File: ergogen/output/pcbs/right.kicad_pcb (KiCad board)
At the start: 2 copper layers, 140.9 x 96.1 mm, 85 parts

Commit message: add: component placement, niceview, mirror pcb
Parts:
- moved LED1 280.0 mm to (330.0, 177.3)
- moved LED2 280.0 mm to (330.0, 159.3)
- moved LED3 280.0 mm to (330.0, 141.3)
- moved S1 280.0 mm to (330.0, 182.0)
- moved S2 280.0 mm to (330.0, 164.0)
- moved S3 280.0 mm to (330.0, 146.0)
- moved D1 264.0 mm to (322.0, 177.6), turned to -90 degrees
- moved D2 264.0 mm to (322.0, 159.6), turned to -90 degrees
- moved D3 264.0 mm to (322.0, 141.6), turned to -90 degrees
- moved H2 262.0 mm to (321.0, 144.0)
- moved LED26 262.0 mm to (321.0, 151.5)
- moved LED27 262.0 mm to (321.0, 172.5)
- moved H3 261.6 mm to (320.8, 188.0)
- moved LED4 244.0 mm to (312.0, 173.3)
- moved LED5 244.0 mm to (312.0, 155.3)
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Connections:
- net close_thumb renamed mirror_close_thumb
- net home_thumb renamed mirror_home_thumb
- net index_bottom renamed mirror_index_bottom
- net index_home renamed mirror_index_home
- net index_top renamed mirror_index_top
- net inner_bottom renamed mirror_inner_bottom
- net inner_home renamed mirror_inner_home
- net inner_thumb renamed mirror_inner_thumb
- net inner_top renamed mirror_inner_top
- net middle_bottom renamed mirror_middle_bottom
- net middle_home renamed mirror_middle_home
- net middle_top renamed mirror_middle_top
- net outer_bottom renamed mirror_outer_bottom
- net outer_home renamed mirror_outer_home
- net outer_thumb renamed mirror_outer_thumb
- net outer_top renamed mirror_outer_top
- net pinky_bottom renamed mirror_pinky_bottom
- net pinky_home renamed mirror_pinky_home
- net pinky_top renamed mirror_pinky_top
- net ring_bonus renamed mirror_ring_bonus
- net ring_bottom renamed mirror_ring_bottom
- net ring_home renamed mirror_ring_home
- net ring_top renamed mirror_ring_top
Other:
- outline, holes or cut-outs redrawn

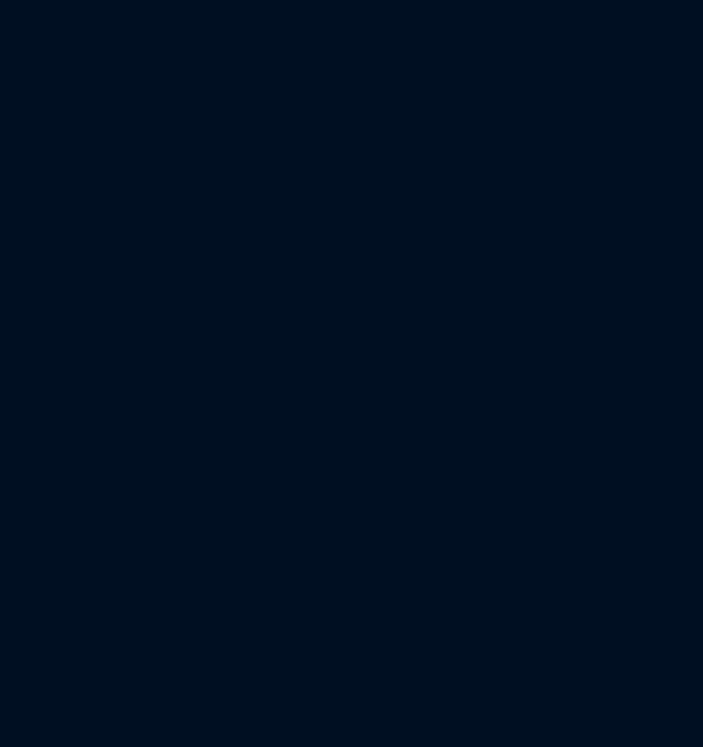
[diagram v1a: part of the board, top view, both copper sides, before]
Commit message: fix: ergogen lio logo
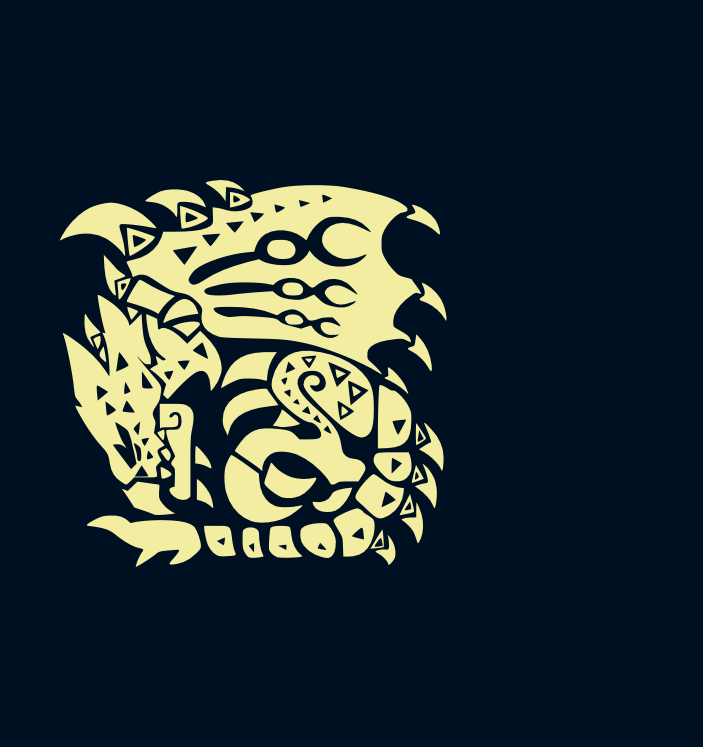
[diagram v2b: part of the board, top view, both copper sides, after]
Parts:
- added G: Lio, custom:lio, F.Cu at (156.2, 173.4)

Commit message: add: routing paras, position adjustments
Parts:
- G: moved to B.Cu
- moved D23 71.4 mm to (325.0, 141.6)
- moved D18 69.7 mm to (276.0, 182.6)
- moved D22 59.3 mm to (253.6, 142.6), turned to -90 degrees
- moved D13 44.8 mm to (250.0, 160.6)
- moved D15 43.9 mm to (232.0, 164.6)
- moved D6 43.9 mm to (286.0, 177.6)
- moved D10 36.7 mm to (268.0, 155.6)
- moved D3 36.7 mm to (304.0, 173.6)
- moved D14 36.0 mm to (250.0, 124.6)
- moved D20 20.9 mm to (237.1, 183.2), turned to -75 degrees
- moved D21 20.9 mm to (217.0, 189.3), turned to -60 degrees
- moved D11 18.0 mm to (268.0, 137.6)
- moved D12 18.0 mm to (268.0, 119.6)
- moved D16 18.0 mm to (232.0, 146.6)
- moved D17 18.0 mm to (232.0, 128.6)
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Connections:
- D1 pad 1: (no net) -> P022
- D10 pad 1: (no net) -> P022
- D10 pad 2: mirror_ring_top -> mirror_middle_bottom
- D11 pad 1: (no net) -> P020
- D11 pad 2: mirror_middle_bottom -> mirror_middle_home
- D12 pad 1: (no net) -> P017
- D12 pad 2: mirror_middle_home -> mirror_middle_top
- D13 pad 1: (no net) -> P022
- D13 pad 2: mirror_middle_top -> mirror_index_bottom
- D14 pad 1: (no net) -> P017
- D14 pad 2: mirror_index_bottom -> mirror_index_top
- D15 pad 1: (no net) -> P022
- D15 pad 2: mirror_index_top -> mirror_inner_bottom
- D16 pad 1: (no net) -> P020
- D16 pad 2: mirror_inner_bottom -> mirror_inner_home
- D17 pad 1: (no net) -> P017
- D17 pad 2: mirror_inner_home -> mirror_inner_top
- D18 pad 1: (no net) -> P017
- D18 pad 2: mirror_inner_top -> mirror_inner_thumb
- D19 pad 1: (no net) -> P017
- D19 pad 2: mirror_inner_thumb -> mirror_close_thumb
- D2 pad 1: (no net) -> P020
- D20 pad 1: (no net) -> P017
- D20 pad 2: mirror_close_thumb -> mirror_home_thumb
- D21 pad 1: (no net) -> P017
- D21 pad 2: mirror_home_thumb -> mirror_outer_thumb
- D22 pad 1: (no net) -> P020
- D22 pad 2: mirror_outer_thumb -> mirror_index_home
- D23 pad 1: (no net) -> P017
- D23 pad 2: mirror_index_home -> mirror_outer_top
- D3 pad 1: (no net) -> P022
- D3 pad 2: mirror_outer_top -> mirror_pinky_bottom
- D4 pad 1: (no net) -> P020
- D4 pad 2: mirror_pinky_bottom -> mirror_pinky_home
- D5 pad 1: (no net) -> P017
- D5 pad 2: mirror_pinky_home -> mirror_pinky_top
- D6 pad 1: (no net) -> P024
- D6 pad 2: mirror_pinky_top -> mirror_ring_bonus
- D7 pad 1: (no net) -> P022
- D7 pad 2: mirror_ring_bonus -> mirror_ring_bottom
- D8 pad 1: (no net) -> P020
- D8 pad 2: mirror_ring_bottom -> mirror_ring_home
- D9 pad 1: (no net) -> P017
- D9 pad 2: mirror_ring_home -> mirror_ring_top
- LED1 pad 2: (no net) -> LED_23
- LED1 pad 4: (no net) -> LED_22
- LED10 pad 2: (no net) -> LED_14
- LED10 pad 4: (no net) -> LED_13
- LED11 pad 2: (no net) -> LED_11
- LED11 pad 4: (no net) -> LED_10
- LED12 pad 2: (no net) -> LED_12
- LED12 pad 4: (no net) -> LED_11
- LED13 pad 2: (no net) -> LED_13
- LED13 pad 4: (no net) -> LED_12
- LED14 pad 2: (no net) -> LED_7
- LED14 pad 4: (no net) -> LED_6
- LED15 pad 2: (no net) -> LED_6
- LED15 pad 4: (no net) -> LED_5
- LED16 pad 2: (no net) -> LED_5
- LED16 pad 4: (no net) -> LED_4
- LED17 pad 2: (no net) -> LED_2
- LED17 pad 4: (no net) -> LED_1
- LED18 pad 2: (no net) -> LED_3
- LED18 pad 4: (no net) -> LED_2
- LED19 pad 2: (no net) -> LED_4
- LED19 pad 4: (no net) -> LED_3
- LED2 pad 2: (no net) -> LED_22
- LED2 pad 4: (no net) -> LED_21
- LED20 pad 2: (no net) -> LED_10
- LED20 pad 4: (no net) -> LED_9
- LED21 pad 2: (no net) -> LED_9
- LED21 pad 4: (no net) -> LED_8
- LED22 pad 2: (no net) -> LED_8
- LED22 pad 4: (no net) -> LED_7
- LED23 pad 2: (no net) -> LED_1
- LED23 pad 4: (no net) -> ULED_6
- LED24 pad 4: LED -> P006
- LED3 pad 2: (no net) -> LED_21
- LED3 pad 4: (no net) -> LED_20
- LED4 pad 2: (no net) -> LED_18
- LED4 pad 4: (no net) -> LED_17
- LED5 pad 2: (no net) -> LED_19
- LED5 pad 4: (no net) -> LED_18
- LED6 pad 2: (no net) -> LED_20
- LED6 pad 4: (no net) -> LED_19
- LED7 pad 2: (no net) -> LED_17
- LED7 pad 4: (no net) -> LED_16
- LED8 pad 2: (no net) -> LED_16
- LED8 pad 4: (no net) -> LED_15
- LED9 pad 2: (no net) -> LED_15
- LED9 pad 4: (no net) -> LED_14
- S1 pad 1: (no net) -> P031
- S10 pad 1: (no net) -> P002
- S11 pad 1: (no net) -> P115
- S12 pad 1: (no net) -> P115
- S13 pad 1: (no net) -> P115
- S14 pad 1: (no net) -> P113
- S15 pad 1: (no net) -> P113
- S16 pad 1: (no net) -> P113
- S17 pad 1: (no net) -> P111
- S18 pad 1: (no net) -> P111
- S19 pad 1: (no net) -> P111
- S2 pad 1: (no net) -> P031
- S20 pad 1: (no net) -> P115
- S21 pad 1: (no net) -> P111
- S22 pad 1: (no net) -> P113
- S23 pad 1: (no net) -> P111
- S3 pad 1: (no net) -> P031
- S4 pad 1: (no net) -> P029
- S5 pad 1: (no net) -> P029
- S6 pad 1: (no net) -> P029
- S7 pad 1: (no net) -> P002
- S8 pad 1: (no net) -> P002
- S9 pad 1: (no net) -> P002

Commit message: update: nice_view pins
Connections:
- ? pad 1: P006 -> P104
- ? pad 4: P020 -> P011
- ? pad 5: P017 -> P100
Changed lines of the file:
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@@
         (fp_text user GND (at 3.5 2.54 270) (layer B.SilkS) (effects (font (size 0.8 0.8) (thickness 0.15)) (justify mirror)))
         (fp_text user CS (at 3.5 5.08 270) (layer B.SilkS) (effects (font (size 0.8 0.8) (thickness 0.15)) (justify mirror)))
-        (pad 5 thru_hole oval (at 1.3 -5.08 360) (size 1.7 1.7) (drill 1) (layers *.Cu *.Mask) (net 32 "P017"))
-        (pad 4 thru_hole oval (at 1.3 -2.54 360) (size 1.7 1.7) (drill 1) (layers *.Cu *.Mask) (net 31 "P020"))
+        (pad 5 thru_hole oval (at 1.3 -5.08 360) (size 1.7 1.7) (drill 1) (layers *.Cu *.Mask) (net 71 "P100"))
+        (pad 4 thru_hole oval (at 1.3 -2.54 360) (size 1.7 1.7) (drill 1) (layers *.Cu *.Mask) (net 72 "P011"))
         (pad 3 thru_hole oval (at 1.3 0.00 360) (size 1.7 1.7) (drill 1) (layers *.Cu *.Mask) (net 34 "VCC"))
         (pad 2 thru_hole rect (at 1.3 2.54 360) (size 1.7 1.7) (drill 1) (layers *.Cu *.Mask) (net 36 "GND"))
-        (pad 1 thru_hole oval (at 1.3 5.08 360) (size 1.7 1.7) (drill 1) (layers *.Cu *.Mask) (net 60 "P006"))
+        (pad 1 thru_hole oval (at 1.3 5.08 360) (size 1.7 1.7) (drill 1) (layers *.Cu *.Mask) (net 73 "P104"))
         )
   (footprint "ceoloide:mounting_hole_plated"

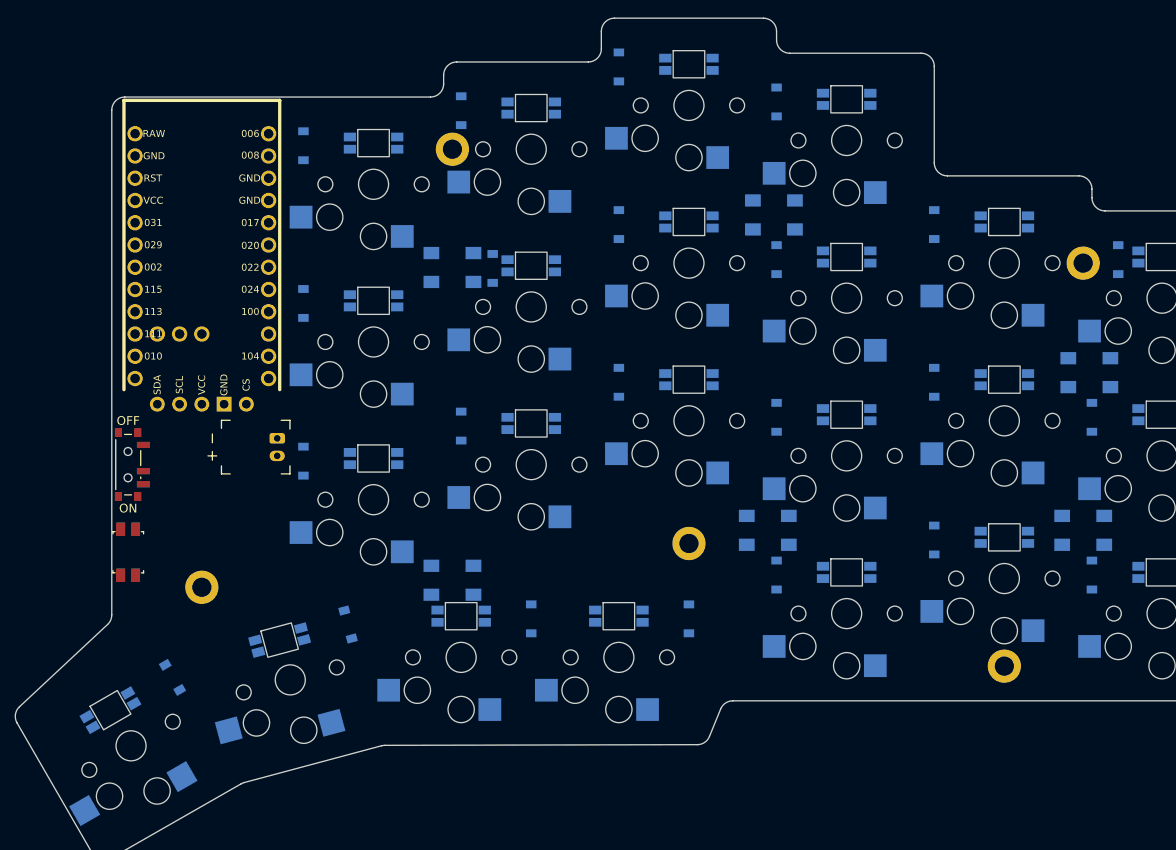
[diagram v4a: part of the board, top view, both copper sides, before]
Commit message: fix: diode / hole / led placement
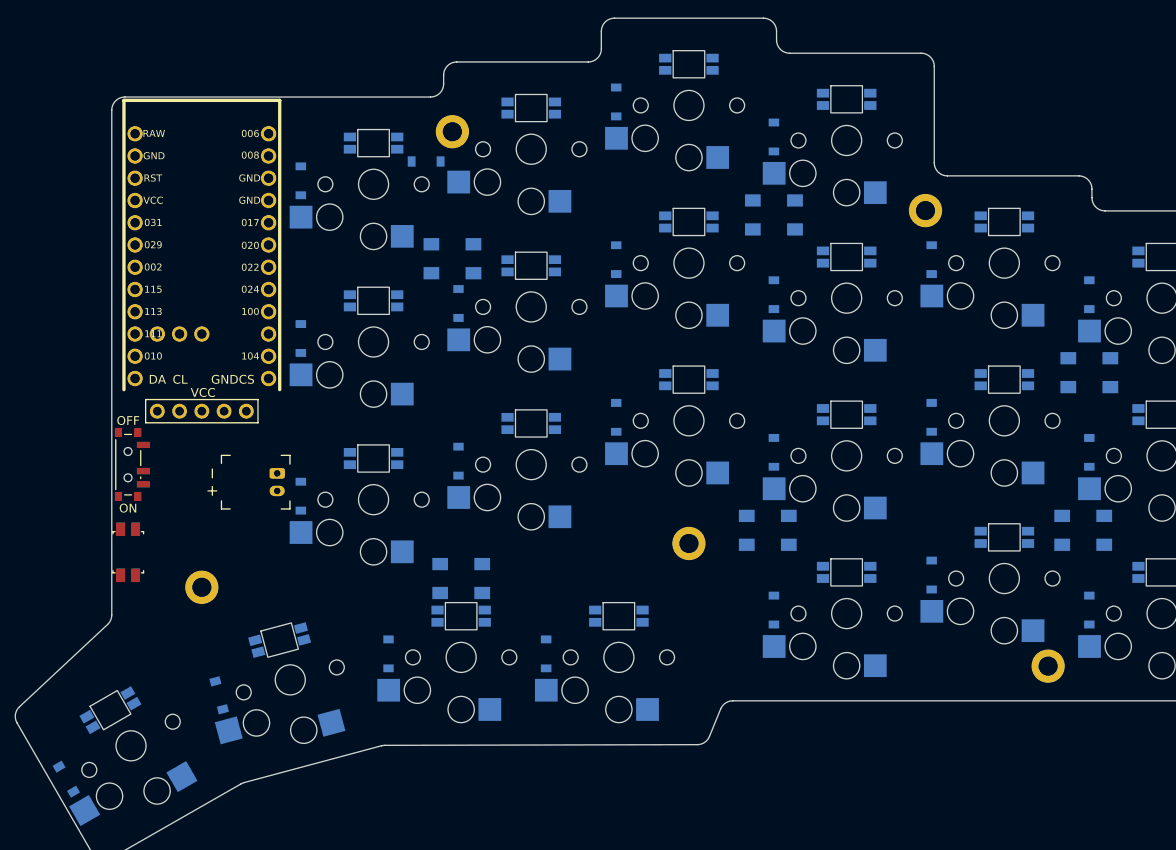
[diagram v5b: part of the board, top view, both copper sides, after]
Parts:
- removed ?: , lib:niceView_headers
- added DISP1: , ceoloide:display_nice_view, F.Cu at (220.4, 142.2)
- moved D23 79.8 mm to (246.0, 130.4), turned to 0 degrees
- moved D22 75.9 mm to (204.9, 200.9), turned to -60 degrees
- moved D18 66.8 mm to (231.7, 132.6)
- moved D13 41.0 mm to (267.7, 123.6)
- moved D6 40.1 mm to (303.7, 141.6)
- moved D14 40.0 mm to (249.7, 164.6)
- moved D10 33.1 mm to (285.7, 127.6)
- moved D3 33.1 mm to (321.7, 145.6)
- moved D15 25.2 mm to (249.7, 146.6)
- moved D11 22.0 mm to (267.7, 159.6)
- moved D12 22.0 mm to (267.7, 141.6)
- moved D16 22.0 mm to (231.7, 168.6)
- moved D17 22.0 mm to (231.7, 150.6)
- moved D4 22.0 mm to (303.7, 177.6)
- moved D5 22.0 mm to (303.7, 159.6)
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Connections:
- D10 pad 1: P022 -> P017
- D10 pad 2: mirror_middle_bottom -> mirror_ring_top
- D11 pad 1: P020 -> P022
- D11 pad 2: mirror_middle_home -> mirror_middle_bottom
- D12 pad 1: P017 -> P020
- D12 pad 2: mirror_middle_top -> mirror_middle_home
- D13 pad 1: P022 -> P017
- D13 pad 2: mirror_index_bottom -> mirror_middle_top
- D14 pad 1: P017 -> P022
- D14 pad 2: mirror_index_top -> mirror_index_bottom
- D15 pad 1: P022 -> P020
- D15 pad 2: mirror_inner_bottom -> mirror_index_home
- D16 pad 1: P020 -> P022
- D16 pad 2: mirror_inner_home -> mirror_inner_bottom
- D17 pad 1: P017 -> P020
- D17 pad 2: mirror_inner_top -> mirror_inner_home
- D18 pad 2: mirror_inner_thumb -> mirror_inner_top
- D19 pad 2: mirror_close_thumb -> mirror_inner_thumb
- D20 pad 2: mirror_home_thumb -> mirror_close_thumb
- D21 pad 2: mirror_outer_thumb -> mirror_home_thumb
- D22 pad 1: P020 -> P017
- D22 pad 2: mirror_index_home -> mirror_outer_thumb
- D23 pad 2: mirror_outer_top -> mirror_index_top
- D3 pad 1: P022 -> P017
- D3 pad 2: mirror_pinky_bottom -> mirror_outer_top
- D4 pad 1: P020 -> P022
- D4 pad 2: mirror_pinky_home -> mirror_pinky_bottom
- D5 pad 1: P017 -> P020
- D5 pad 2: mirror_pinky_top -> mirror_pinky_home
- D6 pad 1: P024 -> P017
- D6 pad 2: mirror_ring_bonus -> mirror_pinky_top
- D7 pad 1: P022 -> P024
- D7 pad 2: mirror_ring_bottom -> mirror_ring_bonus
- D8 pad 1: P020 -> P022
- D8 pad 2: mirror_ring_home -> mirror_ring_bottom
- D9 pad 1: P017 -> P020
- D9 pad 2: mirror_ring_top -> mirror_ring_home
- LED24 pad 1: (no net) -> VCC
- LED25 pad 1: (no net) -> VCC
- LED26 pad 1: (no net) -> VCC
- LED27 pad 1: (no net) -> VCC
- LED28 pad 1: (no net) -> VCC
- LED29 pad 1: (no net) -> VCC
